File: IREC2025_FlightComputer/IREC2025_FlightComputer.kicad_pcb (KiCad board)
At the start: 4 copper layers, 72.5 x 105.8 mm, 143 parts, among them J1 Molex Microfit, J2 BOOT0, J4 Conn_02x03_Counter_Clockwise, Q1 SI7232DN-T1-GE3, U1 STM32U575VGTx, U10 PE4259-63, U11 SX1262IMLTRT, U12 ADXL375BCCZ-RL7, U13 MMC5983MA, U14 BMI088, U15 TMP275AIDGKR VSSOP8, U16 MS5607-02BA, U18 SAM-M10Q-00B, U2 NRVB120VLSFT1G, U4 NRVB120VLSFT1G, U5 LP5912Q3.3DRVRQ1, U7 THGBMUG6C1LBAIL, U8 TPS62153, U9 SN74HCT125DR, X1 1XXD32000MBA, X2 1XXD32000MBA

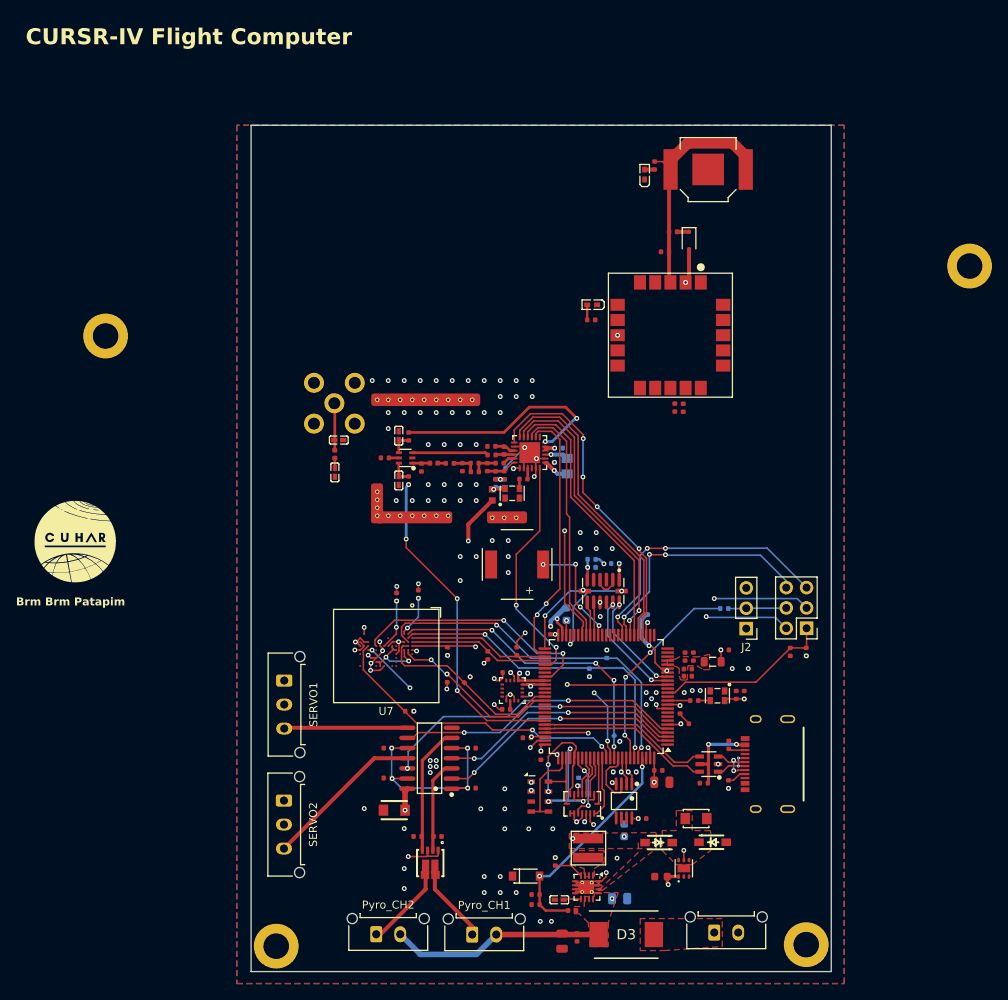
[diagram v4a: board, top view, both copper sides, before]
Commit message: Layout change
Layout changes (Particularly GNSS and LoRa)
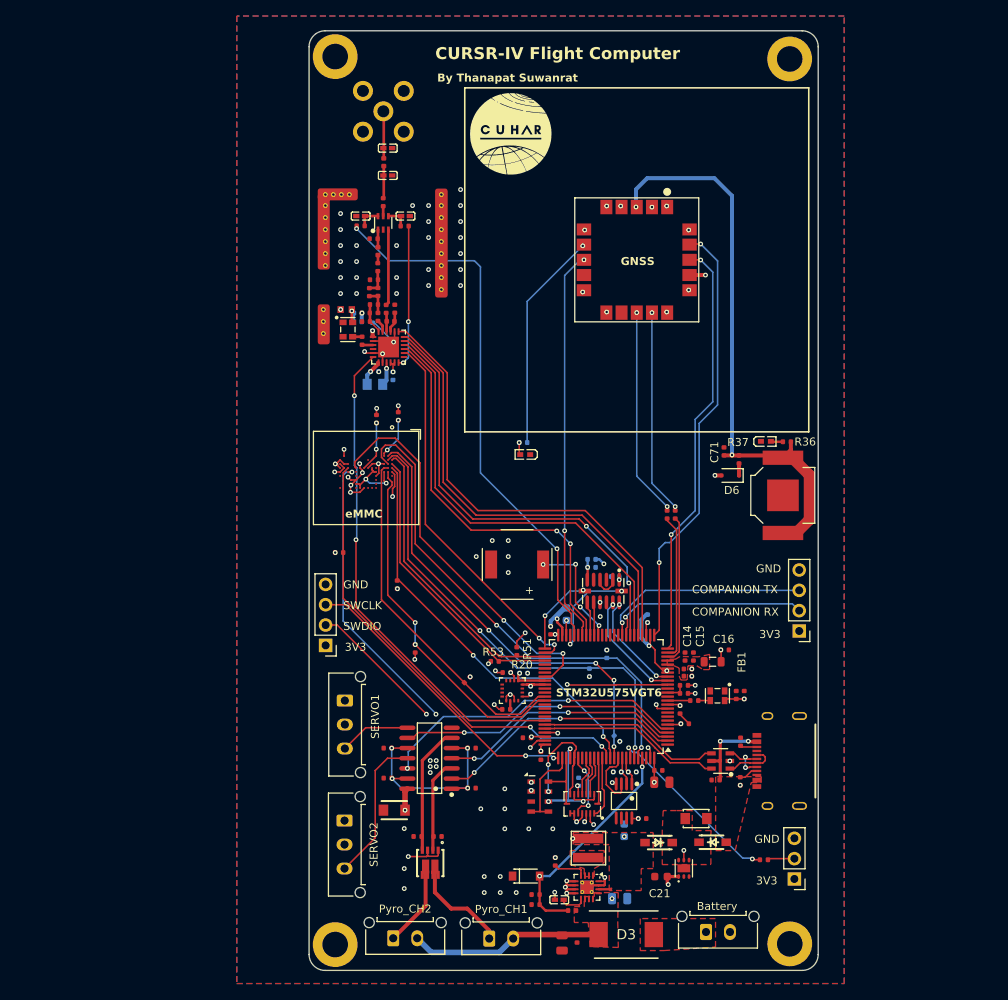
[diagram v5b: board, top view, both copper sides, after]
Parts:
- removed J4: Conn_02x03_Counter_Clockwise, Connector_PinHeader_2.54mm:PinHeader_2x03_P2.54mm_Vertical
- added J3: Companion, Connector_PinHeader_2.54mm:PinHeader_1x04_P2.54mm_Vertical, F.Cu at (120.0, 99.8)
- added J5: SWD, Connector_PinHeader_2.54mm:PinHeader_1x04_P2.54mm_Vertical, F.Cu at (60.8, 101.6)
- R35: moved to B.Cu
- R9: moved to F.Cu
- moved LOGO 74.6 mm to (83.9, 37.7)
- moved H4 45.2 mm to (62.0, 28.0)
- moved BT1 41.8 mm to (118.0, 82.8), turned to 90 degrees
- moved R36 38.3 mm to (118.5, 76.2), turned to 0 degrees
- moved C46 37.7 mm to (68.6, 42.9), turned to 180 degrees
- moved RF1 37.0 mm to (68.0, 34.8)
- moved C47 37.0 mm to (68.6, 39.4)
- moved L9 37.0 mm to (68.1, 41.2)
- moved LED2 36.6 mm to (115.8, 76.1), turned to 0 degrees
- moved H3 34.3 mm to (118.8, 28.3)
- moved C48 33.4 mm to (65.2, 47.9), turned to 0 degrees
- moved R23 32.4 mm to (65.2, 49.2), turned to 0 degrees
- moved C27 32.0 mm to (68.0, 46.2), turned to 90 degrees
- moved J2 31.9 mm to (119.4, 130.8)
- moved R9 31.8 mm to (115.6, 128.4)
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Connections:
- U1 pad 46: unconnected-(U1-PE15-Pad46) -> ANT_SW
- U1 pad 55: LORA_DIO3 -> unconnected-(U1-PD8-Pad55)
- U1 pad 69: ANT_SW -> LORA_DIO3
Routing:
- net GNSS_INT: track 0.00 -> 54.8 mm, vias 0 -> 2
- net GNSS_RST: track 0.00 -> 52.9 mm, vias 0 -> 2
- net Backup: track 30.5 -> 71.9 mm, vias 0 -> 2
- net GNSS_SAFEBOOT: track 14.1 -> 49.2 mm
- net LORA_DIO3: track 29.1 -> 61.9 mm
- net PPS: track 0.00 -> 27.7 mm, vias 0 -> 1
- net ANT_SW: track 41.8 -> 68.8 mm, vias 4 -> 2
- net Net-(U18-TXD): track 0.00 -> 26.3 mm, vias 0 -> 2
- net Net-(U18-RXD): track 0.00 -> 25.9 mm, vias 0 -> 2
- net eMMC_CLK: track 43.2 -> 67.9 mm
- net DAT7: track 21.7 -> 44.2 mm
- net LoRa_MISO: track 34.9 -> 56.1 mm
- net LoRa_RST: track 31.1 -> 51.7 mm, vias 0 -> 2
- net DAT6: track 24.3 -> 44.4 mm
- net eMMC_CMD: track 38.7 -> 58.3 mm
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- added copper zone on F.Cu, net VBUS
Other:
- board size 72.5 x 105.8 mm -> 63.6 x 117.5 mm
- board text added: "3V3"
- board text added: "Battery"
- board text added: "By Thanapat Suwanrat"
- board text added: "C14"
- board text added: "C15"
- board text added: "C16"
- board text added: "C21"
- board text added: "C71"
- board text added: "COMPANION RX"
- board text added: "COMPANION TX"
- board text added: "D6"
- board text added: "FB1"
- board text added: "GND"
- board text added: "GNSS"
- board text added: "R20"
- board text added: "R36"
- board text added: "R37"
- board text added: "R51"
- board text added: "R53"
- board text added: "STM32U575VGT6"
- board text added: "SWCLK"
- board text added: "SWDIO"
- board text added: "eMMC"
- board text removed: "Brm Brm Patapim"

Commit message: Added via stitching
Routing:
- net LoRa_NSS: track 59.0 -> 55.2 mm
- net LoRa_MOSI: track 56.5 -> 52.8 mm
- net LoRa_SCLK: track 57.4 -> 53.7 mm
- net LoRa_MISO: track 56.1 -> 52.5 mm
- net LoRa_RST: track 51.7 -> 48.0 mm
- net VBAT-: track 93.6 -> 95.5 mm, vias 104 -> 252
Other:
- board text added: "R33"
- board text added: "R34"
- board text added: "X1"
